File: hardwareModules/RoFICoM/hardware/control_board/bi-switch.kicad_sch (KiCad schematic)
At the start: 11 parts, among them Q1 AONR21357, Q2 PNM723T703E0-2, Q3 AONR21357, U6 ACS70331

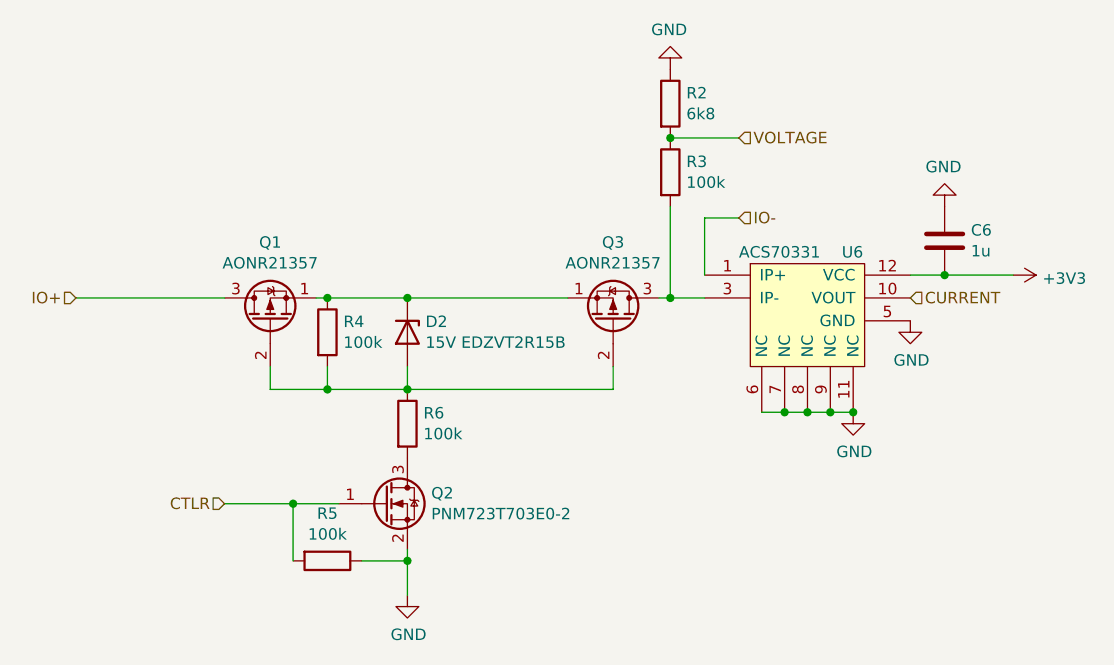
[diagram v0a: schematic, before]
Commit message: roficom: Implement v1 hardware
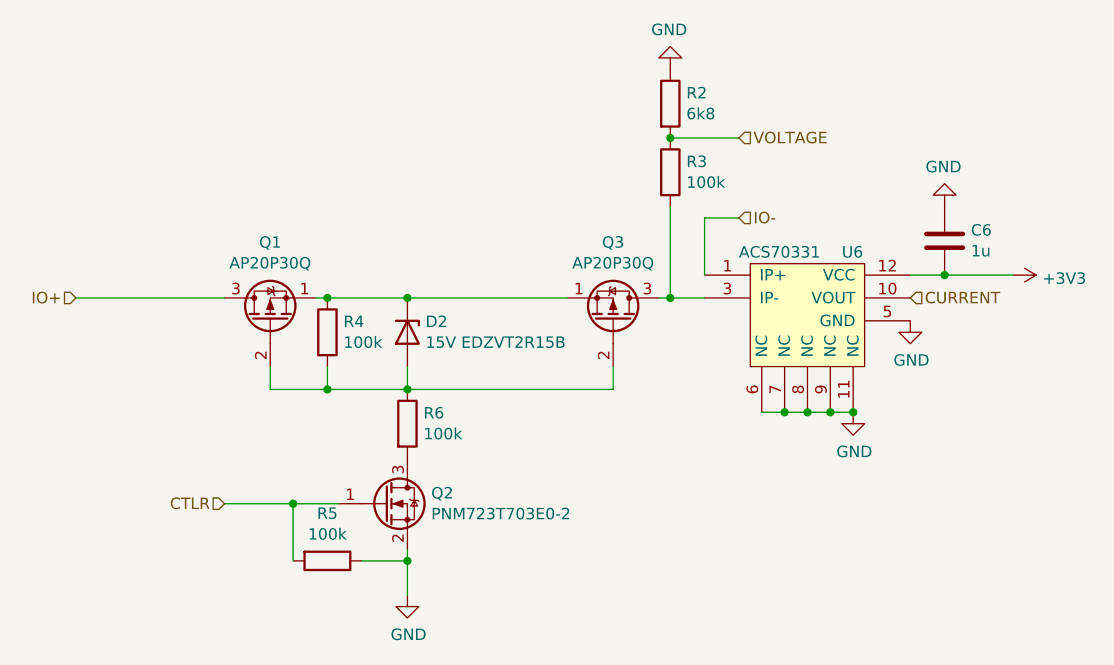
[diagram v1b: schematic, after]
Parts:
- Q1, Q3: value AONR21357 -> AP20P30Q; LCSC C431196 -> C2837278
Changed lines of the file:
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@@
-(kicad_sch (version 20210621) (generator eeschema)
+(kicad_sch (version 20211123) (generator eeschema)
   (paper "A4")
-  (junction (at 152.4 76.2) (diameter 0) (color 0 0 0 0))
-  (junction (at 123.19 105.41) (diameter 0) (color 0 0 0 0))
-  (junction (at 167.64 88.9) (diameter 0) (color 0 0 0 0))
-  (junction (at 170.18 88.9) (diameter 0) (color 0 0 0 0))
-  (junction (at 182.88 73.66) (diameter 0) (color 0 0 0 0))
-  (junction (at 172.72 88.9) (diameter 0) (color 0 0 0 0))
-  (junction (at 165.1 88.9) (diameter 0) (color 0 0 0 0))
-  (junction (at 123.19 76.2) (diameter 0) (color 0 0 0 0))
-  (junction (at 123.19 86.36) (diameter 0) (color 0 0 0 0))
-  (junction (at 114.3 86.36) (diameter 0) (color 0 0 0 0))
-  (junction (at 152.4 58.42) (diameter 0) (color 0 0 0 0))
-  (junction (at 110.49 99.06) (diameter 0) (color 0 0 0 0))
-  (junction (at 114.3 76.2) (diameter 0) (color 0 0 0 0))
+  (junction (at 167.64 88.9) (diameter 0) (color 0 0 0 0)
+  )
+  (junction (at 114.3 76.2) (diameter 0) (color 0 0 0 0)
+  )
+  (junction (at 172.72 88.9) (diameter 0) (color 0 0 0 0)
+  )
+  (junction (at 152.4 58.42) (diameter 0) (color 0 0 0 0)
+  )
+  (junction (at 152.4 76.2) (diameter 0) (color 0 0 0 0)
+  )
+  (junction (at 114.3 86.36) (diameter 0) (color 0 0 0 0)
+  )
+  (junction (at 110.49 99.06) (diameter 0) (color 0 0 0 0)
+  )
+  (junction (at 182.88 73.66) (diameter 0) (color 0 0 0 0)
+  )
+  (junction (at 123.19 86.36) (diameter 0) (color 0 0 0 0)
+  )
+  (junction (at 123.19 105.41) (diameter 0) (color 0 0 0 0)
+  )
+  (junction (at 123.19 76.2) (diameter 0) (color 0 0 0 0)
+  )
+  (junction (at 165.1 88.9) (diameter 0) (color 0 0 0 0)
+  )
+  (junction (at 170.18 88.9) (diameter 0) (color 0 0 0 0)
+  )
   (wire (pts (xy 160.02 67.31) (xy 156.21 67.31))
     (stroke (width 0) (type default) (color 0 0 0 0))
@@
     (effects (font (size 1.27 1.27)) (justify left))
   )
-  (symbol (lib_id "rofi:ACS70331") (at 167.64 76.2 0)
+  (symbol (lib_id "rofi:ACS70331") (at 167.64 76.2 0) (unit 1)
     (in_bom yes) (on_board yes)
     (property "Reference" "U6" (id 0) (at 171.45 71.12 0)
@@
     (pin "9")
   )
-  (symbol (lib_id "Device:Q_PMOS_SGD") (at 107.95 78.74 90)
+  (symbol (lib_id "Device:Q_PMOS_SGD") (at 107.95 78.74 90) (unit 1)
     (in_bom yes) (on_board yes)
     (property "Reference" "Q1" (id 0) (at 107.95 70.0278 90))
-    (property "Value" "AONR21357" (id 1) (at 107.95 72.3392 90))
+    (property "Value" "AP20P30Q" (id 1) (at 107.95 72.3392 90))
     (property "Footprint" "rofi:DFN3.3X3.3-EP" (id 2) (at 105.41 73.66 0)
       (effects (font (size 1.27 1.27)) hide)
@@
       (effects (font (size 1.27 1.27)) hide)
     )
-    (property "LCSC" "C431196" (id 4) (at 107.95 78.74 90)
+    (property "LCSC" "C2837278" (id 4) (at 107.95 78.74 90)
       (effects (font (size 1.27 1.27)) hide)
     )
@@
     (pin "3")
   )
-  (symbol (lib_id "Device:D_Zener") (at 123.19 80.01 270)
+  (symbol (lib_id "Device:D_Zener") (at 123.19 80.01 270) (unit 1)
     (in_bom yes) (on_board yes)
     (property "Reference" "D2" (id 0) (at 125.1966 78.8416 90)
@@
     (pin "2")
   )
-  (symbol (lib_id "Device:R") (at 114.3 80.01 0)
+  (symbol (lib_id "Device:R") (at 114.3 80.01 0) (unit 1)
     (in_bom yes) (on_board yes)
     (property "Reference" "R4" (id 0) (at 116.078 78.8416 0)
@@
     (pin "2")
   )
-  (symbol (lib_id "Device:R") (at 123.19 90.17 0)
+  (symbol (lib_id "Device:R") (at 123.19 90.17 0) (unit 1)
     (in_bom yes) (on_board yes)
     (property "Reference" "R6" (id 0) (at 124.968 89.0016 0)
@@
     (pin "2")
   )
-  (symbol (lib_id "Device:R") (at 114.3 105.41 270)
+  (symbol (lib_id "Device:R") (at 114.3 105.41 270) (unit 1)
     (in_bom yes) (on_board yes)
     (property "Reference" "R5" (id 0) (at 114.3 100.1522 90))
@@
     (pin "2")
   )
-  (symbol (lib_id "power:GND") (at 123.19 109.22 0)
+  (symbol (lib_id "power:GND") (at 123.19 109.22 0) (unit 1)
     (in_bom yes) (on_board yes)
     (property "Reference" "#PWR0130" (id 0) (at 123.19 115.57 0)
@@
     (pin "1")
   )
-  (symbol (lib_id "Device:R") (at 152.4 62.23 0)
+  (symbol (lib_id "Device:R") (at 152.4 62.23 0) (unit 1)
     (in_bom yes) (on_board yes)
     (property "Reference" "R3" (id 0) (at 154.178 61.0616 0)
@@
     (pin "2")
   )
-  (symbol (lib_id "Device:R") (at 152.4 54.61 0)
+  (symbol (lib_id "Device:R") (at 152.4 54.61 0) (unit 1)
     (in_bom yes) (on_board yes)
     (property "Reference" "R2" (id 0) (at 154.178 53.4416 0)
@@
     (pin "2")
   )
-  (symbol (lib_id "power:GND") (at 152.4 50.8 180)
+  (symbol (lib_id "power:GND") (at 152.4 50.8 180) (unit 1)
     (in_bom yes) (on_board yes)
     (property "Reference" "#PWR0131" (id 0) (at 152.4 44.45 0)
@@
     (pin "1")
   )
-  (symbol (lib_id "power:GND") (at 179.07 78.74 0)
+  (symbol (lib_id "power:GND") (at 179.07 78.74 0) (unit 1)
     (in_bom yes) (on_board yes)
     (property "Reference" "#PWR0132" (id 0) (at 179.07 85.09 0)
@@
     (pin "1")
   )
-  (symbol (lib_id "power:GND") (at 172.72 88.9 0)
+  (symbol (lib_id "power:GND") (at 172.72 88.9 0) (unit 1)
     (in_bom yes) (on_board yes)
     (property "Reference" "#PWR0133" (id 0) (at 172.72 95.25 0)
@@
     (pin "1")
   )
-  (symbol (lib_id "power:+3V3") (at 190.5 73.66 270)
+  (symbol (lib_id "power:+3V3") (at 190.5 73.66 270) (unit 1)
     (in_bom yes) (on_board yes)
     (property "Reference" "#PWR0134" (id 0) (at 186.69 73.66 0)
@@
     (pin "1")
   )
-  (symbol (lib_id "Device:C") (at 182.88 69.85 0)
+  (symbol (lib_id "Device:C") (at 182.88 69.85 0) (unit 1)
     (in_bom yes) (on_board yes)
     (property "Reference" "C6" (id 0) (at 185.801 68.6816 0)
@@
     (pin "2")
   )
-  (symbol (lib_id "power:GND") (at 182.88 66.04 180)
+  (symbol (lib_id "power:GND") (at 182.88 66.04 180) (unit 1)
     (in_bom yes) (on_board yes)
     (property "Reference" "#PWR0135" (id 0) (at 182.88 59.69 0)
@@
     (pin "1")
   )
-  (symbol (lib_id "Device:Q_PMOS_SGD") (at 146.05 78.74 270) (mirror x)
+  (symbol (lib_id "Device:Q_PMOS_SGD") (at 146.05 78.74 270) (mirror x) (unit 1)
     (in_bom yes) (on_board yes)
     (property "Reference" "Q3" (id 0) (at 146.05 70.0278 90))
-    (property "Value" "AONR21357" (id 1) (at 146.05 72.3392 90))
+    (property "Value" "AP20P30Q" (id 1) (at 146.05 72.3392 90))
     (property "Footprint" "rofi:DFN3.3X3.3-EP" (id 2) (at 148.59 73.66 0)
       (effects (font (size 1.27 1.27)) hide)
@@
       (effects (font (size 1.27 1.27)) hide)
     )
-    (property "LCSC" "C431196" (id 4) (at 146.05 78.74 90)
+    (property "LCSC" "C2837278" (id 4) (at 146.05 78.74 90)
       (effects (font (size 1.27 1.27)) hide)
     )
@@
     (pin "3")
   )
-  (symbol (lib_id "Device:Q_NMOS_GSD") (at 120.65 99.06 0)
+  (symbol (lib_id "Device:Q_NMOS_GSD") (at 120.65 99.06 0) (unit 1)
     (in_bom yes) (on_board yes)
     (property "Reference" "Q2" (id 0) (at 125.8316 97.8916 0)

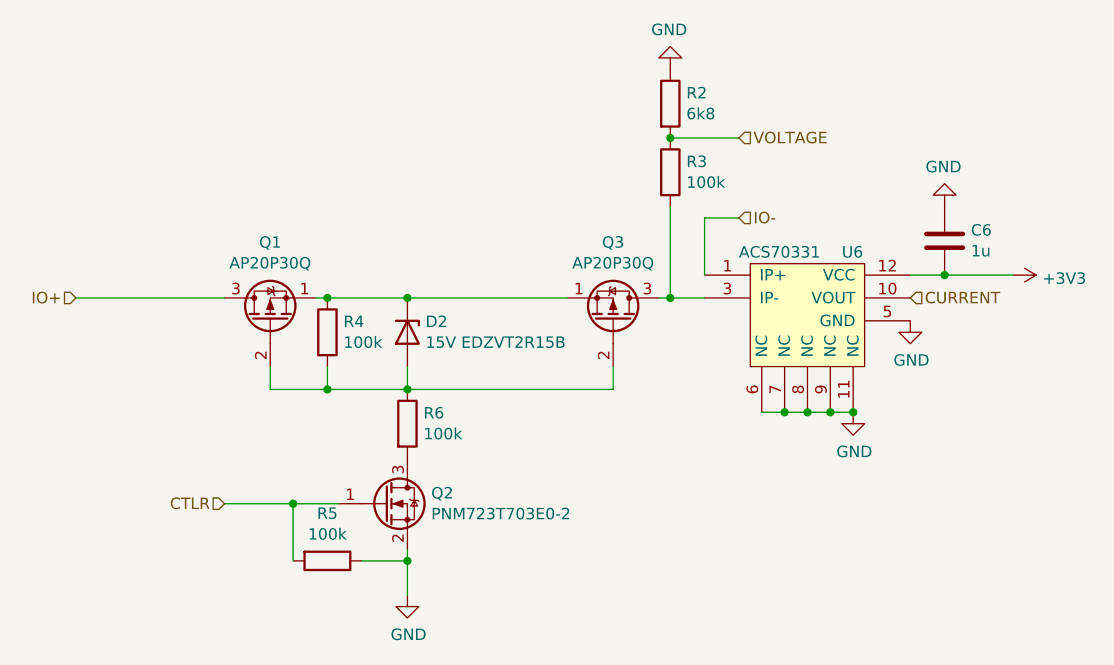
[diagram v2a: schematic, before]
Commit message: roficom: Add Hall position sensor hardware
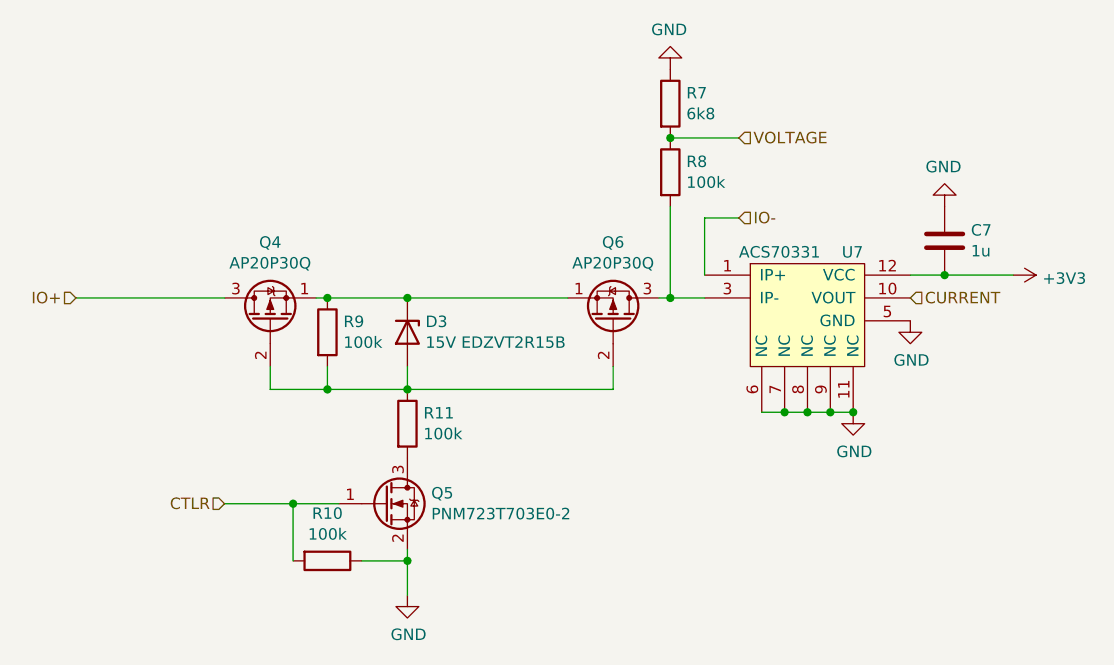
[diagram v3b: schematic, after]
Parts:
- renumbered C6 to C7, D2 to D3, Q1 to Q4, Q2 to Q5, Q3 to Q6, R5 to R10, R6 to R11, R2 to R7, R3 to R8, R4 to R9, U6 to U7
